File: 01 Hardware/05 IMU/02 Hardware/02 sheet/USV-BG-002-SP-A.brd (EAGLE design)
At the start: 70.8 x 50.1 mm, 3 parts, among them J2 690367291276, U1 RASPBERRY_PICOTH

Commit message: Sheet and Board for IMU
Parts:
- added R1: 10k, rcl:M0805
- added X1: MKDSN1,5/3-5,08, con-phoenix-508:MKDSN1,5/3-5,08
- moved U$1 42.6 mm to (45.1, 5.08)
- moved U1 7.38 mm to (31.1, 25.1), turned to 90 degrees
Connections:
- removed net 3V3(OUT): U1.36
- removed net AVR_CTS: J2.8
- removed net AVR_RTS: J2.9
- removed net AVR_RX: J2.7
- removed net AVR_TX: J2.6
- new net LED/IO2: U1.4, X1.2
- new net TA/IO3: R1.2, U1.5, X1.3
- new net UART0_RX: J2.7, U1.2
- new net UART0_TX: J2.6, U1.1
- net +3V3: now also J2.5, U1.36, X1.1
- net +5V: no longer J2.5
- net ERROR1: now also U1.19
- net ERROR2: now also U1.20
- net GND: now also R1.1, U1.37
- net IRQ: now also U1.17
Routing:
- net TA/IO3: track 0.00 -> 40.1 mm
- net LED/IO2: track 0.00 -> 34.4 mm
- net +3V3: track 54.0 -> 84.9 mm, vias 0 -> 1
- net ERROR2: track 13.1 -> 43.5 mm
- net UART0_TX: track 0.00 -> 29.3 mm, vias 0 -> 1
- net AVR_RTS: track 25.8 -> 0.00 mm
- net AVR_CTS: track 25.0 -> 0.00 mm
- net UART0_RX: track 0.00 -> 24.9 mm
- net ERROR1: track 26.2 -> 48.3 mm, vias 0 -> 1
- net IRQ: track 12.8 -> 31.0 mm
- net AVR_TX: track 6.19 -> 0.00 mm
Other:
- board text added: "USV IMU"
- board text added: "USV-BG-002-LP-A"
- board text removed: "USV Modem"
- board text removed: "USV-BG-001-LP-A"

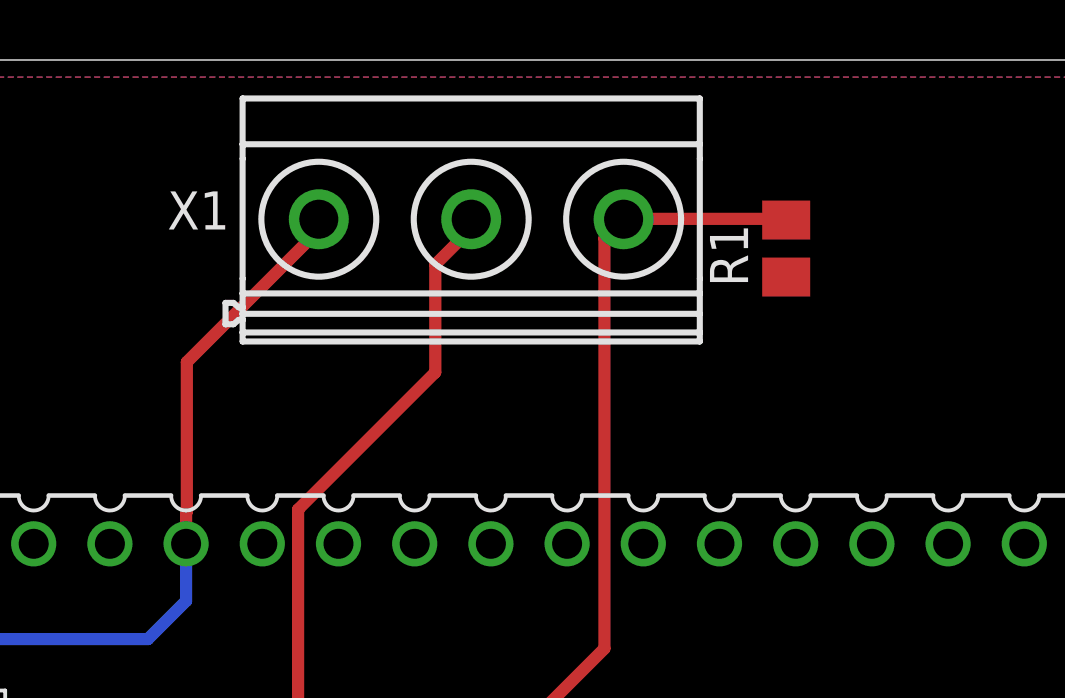
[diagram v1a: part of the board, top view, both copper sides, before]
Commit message: Button with Pullup
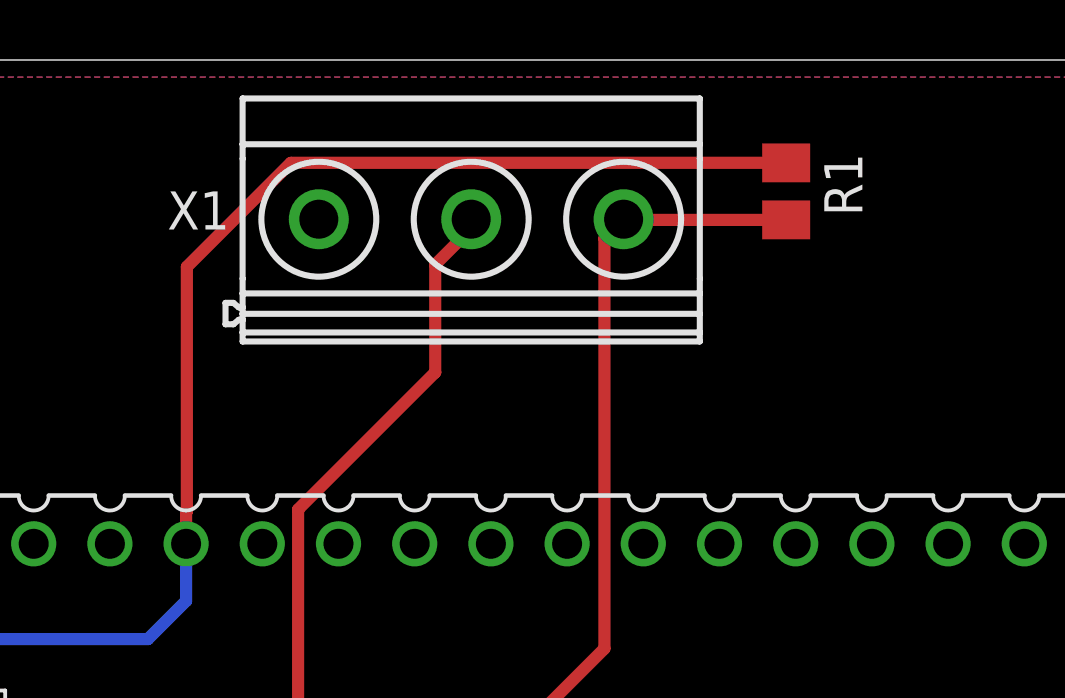
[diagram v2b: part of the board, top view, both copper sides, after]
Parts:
- moved R1 1.91 mm to (37.1, 45.7), turned to 270 degrees
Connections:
- net +3V3: now also R1.1; no longer X1.1
- net GND: now also X1.1; no longer R1.1
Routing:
- net +3V3: track 84.9 -> 102.9 mm
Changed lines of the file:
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@@
 <grid distance="0.0125" unitdist="inch" unit="inch" style="lines" multiple="1" display="no" altdistance="5" altunitdist="mil" altunit="mil"/>
 <layers>
-<layer number="1" name="Top" color="4" fill="1" visible="yes" active="yes"/>
+<layer number="1" name="Top" color="4" fill="1" visible="no" active="yes"/>
 <layer number="2" name="Route2" color="16" fill="1" visible="no" active="no"/>
 <layer number="3" name="Route3" color="17" fill="1" visible="no" active="no"/>
@@
 <layer number="14" name="Route14" color="22" fill="1" visible="no" active="no"/>
 <layer number="15" name="Route15" color="23" fill="1" visible="no" active="no"/>
-<layer number="16" name="Bottom" color="1" fill="1" visible="yes" active="yes"/>
+<layer number="16" name="Bottom" color="1" fill="1" visible="no" active="yes"/>
 <layer number="17" name="Pads" color="2" fill="1" visible="yes" active="yes"/>
 <layer number="18" name="Vias" color="2" fill="1" visible="yes" active="yes"/>
 <layer number="19" name="Unrouted" color="6" fill="1" visible="yes" active="yes"/>
-<layer number="20" name="Dimension" color="24" fill="1" visible="no" active="yes"/>
-<layer number="21" name="tPlace" color="7" fill="1" visible="no" active="yes"/>
+<layer number="20" name="Dimension" color="24" fill="1" visible="yes" active="yes"/>
+<layer number="21" name="tPlace" color="7" fill="1" visible="yes" active="yes"/>
 <layer number="22" name="bPlace" color="7" fill="1" visible="no" active="yes"/>
 <layer number="23" name="tOrigins" color="15" fill="1" visible="no" active="yes"/>
 <layer number="24" name="bOrigins" color="15" fill="1" visible="no" active="yes"/>
-<layer number="25" name="tNames" color="7" fill="1" visible="no" active="yes"/>
+<layer number="25" name="tNames" color="7" fill="1" visible="yes" active="yes"/>
 <layer number="26" name="bNames" color="7" fill="1" visible="no" active="yes"/>
 <layer number="27" name="tValues" color="7" fill="1" visible="no" active="yes"/>
 <layer number="28" name="bValues" color="7" fill="1" visible="no" active="yes"/>
-<layer number="29" name="tStop" color="7" fill="3" visible="no" active="yes"/>
+<layer number="29" name="tStop" color="7" fill="3" visible="yes" active="yes"/>
 <layer number="30" name="bStop" color="7" fill="6" visible="no" active="yes"/>
 <layer number="31" name="tCream" color="7" fill="4" visible="no" active="yes"/>
@@
 <attribute name="VALUE" x="46.6725" y="26.0985" size="1.778" layer="27" rot="R180"/>
 </element>
-<element name="R1" library="rcl" library_urn="urn:adsk.eagle:library:334" package="M0805" package3d_urn="urn:adsk.eagle:package:23556/2" value="10k" x="37.1475" y="43.815" smashed="yes" rot="R90">
-<attribute name="NAME" x="35.8775" y="42.545" size="1.27" layer="25" rot="R90"/>
-<attribute name="POPULARITY" value="45" x="37.1475" y="43.815" size="1.778" layer="27" rot="R90" display="off"/>
-<attribute name="SPICEPREFIX" value="R" x="37.1475" y="43.815" size="1.778" layer="27" rot="R90" display="off"/>
-<attribute name="VALUE" x="39.6875" y="42.545" size="1.27" layer="27" rot="R90"/>
+<element name="R1" library="rcl" library_urn="urn:adsk.eagle:library:334" package="M0805" package3d_urn="urn:adsk.eagle:package:23556/2" value="10k" x="37.1475" y="45.72" smashed="yes" rot="R270">
+<attribute name="NAME" x="38.4175" y="46.99" size="1.27" layer="25" rot="R270"/>
+<attribute name="POPULARITY" value="45" x="37.1475" y="45.72" size="1.778" layer="27" rot="R270" display="off"/>
+<attribute name="SPICEPREFIX" value="R" x="37.1475" y="45.72" size="1.778" layer="27" rot="R270" display="off"/>
+<attribute name="VALUE" x="34.6075" y="46.99" size="1.27" layer="27" rot="R270"/>
 </element>
 <element name="X1" library="con-phoenix-508" library_urn="urn:adsk.eagle:library:176" package="MKDSN1,5/3-5,08" package3d_urn="urn:adsk.eagle:package:9641/1" value="MKDSN1,5/3-5,08" x="29.21" y="44.7675" smashed="yes">
@@
 <contactref element="U1" pad="13"/>
 <contactref element="U1" pad="37"/>
-<contactref element="R1" pad="1"/>
+<contactref element="X1" pad="1"/>
 </signal>
 <signal name="+5V">
@@
 <wire x1="32.4612" y1="2.8956" x2="32.385" y2="2.83" width="0.1524" layer="1"/>
 <contactref element="U1" pad="36"/>
-<contactref element="X1" pad="1"/>
 <wire x1="32.4612" y1="4.1148" x2="32.4612" y2="3.6576" width="0.1524" layer="1"/>
 <wire x1="31.6992" y1="4.8768" x2="32.4612" y2="4.1148" width="0.4064" layer="1"/>
 <wire x1="32.4612" y1="3.6576" x2="32.385" y2="2.83" width="0.1524" layer="1"/>
-<wire x1="21.4884" y1="44.3484" x2="21.4884" y2="44.6532" width="0.4064" layer="1"/>
-<wire x1="17.1704" y1="40.0304" x2="21.4884" y2="44.3484" width="0.4064" layer="1"/>
-<wire x1="17.1704" y1="35.052" x2="17.1704" y2="40.0304" width="0.4064" layer="1"/>
-<wire x1="17.1704" y1="35.052" x2="17.145" y2="35.0266" width="0.4064" layer="1"/>
+<wire x1="17.145" y1="35.0266" x2="17.1704" y2="35.052" width="0.4064" layer="1"/>
 <wire x1="17.145" y1="33.9725" x2="17.145" y2="35.0266" width="0.4064" layer="1"/>
-<wire x1="21.4884" y1="44.6532" x2="21.5689" y2="44.7925" width="0.4064" layer="1"/>
 <via x="31.6992" y="4.8768" extent="1-16" drill="0.35"/>
 <contactref element="J2" pad="5"/>
@@
 <wire x1="4.154715625" y1="8.545284375" x2="4.154715625" y2="30.143028125" width="0.4064" layer="16"/>
 <wire x1="4.154715625" y1="30.143028125" x2="4.8091875" y2="30.7975" width="0.4064" layer="16"/>
+<contactref element="R1" pad="1"/>
+<wire x1="17.1704" y1="43.2054" x2="20.6375" y2="46.6725" width="0.4064" layer="1"/>
+<wire x1="20.6375" y1="46.6725" x2="37.145" y2="46.6725" width="0.4064" layer="1"/>
+<wire x1="37.145" y1="46.6725" x2="37.1475" y2="46.67" width="0.4064" layer="1"/>
+<wire x1="17.1704" y1="35.052" x2="17.1704" y2="43.2054" width="0.4064" layer="1"/>
 </signal>
 <signal name="VSYS">
@@
 <contactref element="R1" pad="2"/>
 <contactref element="X1" pad="3"/>
-<wire x1="37.1475" y1="44.765" x2="37.0332" y2="44.8056" width="0.1524" layer="1"/>
 <wire x1="17.2212" y1="16.6116" x2="17.2212" y2="16.3068" width="0.1524" layer="1"/>
 <wire x1="17.2212" y1="16.6116" x2="31.0896" y2="30.48" width="0.4064" layer="1"/>
 <wire x1="17.2212" y1="16.3068" x2="17.145" y2="16.1925" width="0.1524" layer="1"/>
 <wire x1="31.742" y1="44.8056" x2="31.7289" y2="44.7925" width="0.4064" layer="1"/>
-<wire x1="37.0332" y1="44.8056" x2="31.742" y2="44.8056" width="0.4064" layer="1"/>
 <wire x1="31.0896" y1="44.1532" x2="31.742" y2="44.8056" width="0.4064" layer="1"/>
 <wire x1="31.0896" y1="30.48" x2="31.0896" y2="44.1532" width="0.4064" layer="1"/>
+<wire x1="37.1475" y1="44.77" x2="31.7776" y2="44.77" width="0.4064" layer="1"/>
+<wire x1="31.7776" y1="44.77" x2="31.742" y2="44.8056" width="0.4064" layer="1"/>
 </signal>
 </signals>
